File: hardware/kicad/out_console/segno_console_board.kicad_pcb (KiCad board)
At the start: 2 copper layers, 99.5 x 99.5 mm, 64 parts, among them J1 RaspberryPi_Pico_SMD_HandSold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, J10 JST_XH_B2B-XH-A_1x02_P2.50mm_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, J11 JST_XH_B2B-XH-A_1x02_P2.50mm_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, J12 JST_XH_B2B-XH-A_1x02_P2.50mm_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, J13 JST_XH_B2B-XH-A_1x02_P2.50mm_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, J14 JST_XH_B2B-XH-A_1x02_P2.50mm_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, J15 JST_XH_B2B-XH-A_1x02_P2.50mm_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, J16 JST_XH_B2B-XH-A_1x02_P2.50mm_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, J17 JST_XH_B2B-XH-A_1x02_P2.50mm_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, J18 JST_XH_B2B-XH-A_1x02_P2.50mm_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, J19 JST_XH_B2B-XH-A_1x02_P2.50mm_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, J2 IDC-Header_2x20_P2.54mm_Verti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, J20 JST_XH_B3B-XH-A_1x03_P2.50mm_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, J21 JST_XH_B3B-XH-A_1x03_P2.50mm_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, J22 PinHeader_2x04_P2.54mm_Vertic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, J3 JST_XH_B4B-XH-A_1x04_P2.50mm_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, J4 JST_XH_B3B-XH-A_1x03_P2.50mm_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, J5 JST_XH_B2B-XH-A_1x02_P2.50mm_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, J6 JST_XH_B8B-XH-A_1x08_P2.50mm_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, J7 JST_XH_B3B-XH-A_1x03_P2.50mm_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, J8 JST_XH_B2B-XH-A_1x02_P2.50mm_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, J9 JST_XH_B2B-XH-A_1x02_P2.50mm_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, U1 DIP-14_W7.62mm, U2 DIP-6_W7.62mm

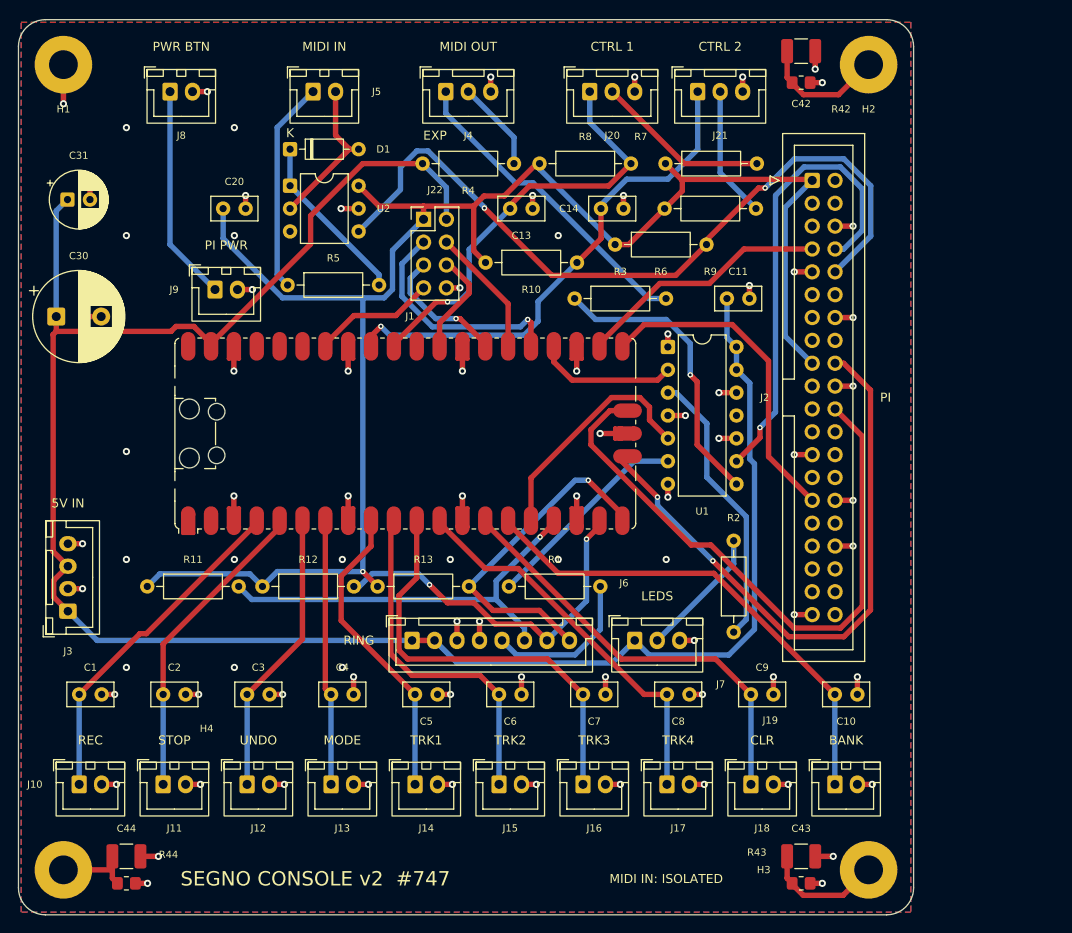
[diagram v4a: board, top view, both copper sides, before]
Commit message: fix(hardware): drop the SMD bond parts, and review the board for manufacture
The six surface-mount parts I added for the optional chassis bonds are gone.
They were a 10 nF cap and a 1 M bleeder per hole, unfitted by default, so EMC
testing could add an RF bond without a respin -- and nothing in through-hole
fits those corners, so they were SMD. That put six surface-mount parts on a
board that is hand-soldered through-hole on purpose, carried by every unit
built, for a bond that may never be wanted. H2/H3/H4 keep the plated pad and
nothing else; if a bond is ever needed a leaded cap solders from the pad to the
nearest ground via, which is a bench job on one board rather than a BOM line on
all of them. CHASSIS_BOND now gates that the other three holes are wired to
NOTHING -- a second path to ground through anything at all fails.

The only SMD left is J1, the Pico module, which is settled.

THE ENCLOSURE NOW MATCHES THE BOARD

The plate was drilling an 85 x 87 M3 rectangle measured off the V1 Pro Micro
board, while this board's holes are on 89.5 x 89.5. Both parts were unordered,
so it cost nothing -- once, and only because someone thought to look. The plate
now drills 89.5 x 89.5, reserves the real 99.5 x 99.5 outline, and the station
is labelled CONSOLE_BOARD rather than MAIN_BOARD, because the V1 board stays
with the standalone pedal.

It is a seam now, not a copied number: console_board_pcb.py writes
out_console/console_board_mount.json and segno_enclosure.py's BOARD_MOUNT gate
reads it -- the mirror of the rear_io_stations.json handoff going the other way.
Both halves of the gate were proven to bite.

WHAT THE FAB REVIEW FOUND

- Silkscreen under the fab's floor. All 58 designators were stroked at 0.133 mm
  against JLCPCB's 0.15 mm minimum, where lines thin, break, or are dropped.
  KiCad's own minimum is 0.08 mm, so its DRC had nothing to say. Stroke is now
  h/5 (0.16 mm at the 0.8 mm text height) and SILK_FAB gates height and stroke.
- Router vias at the fab f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
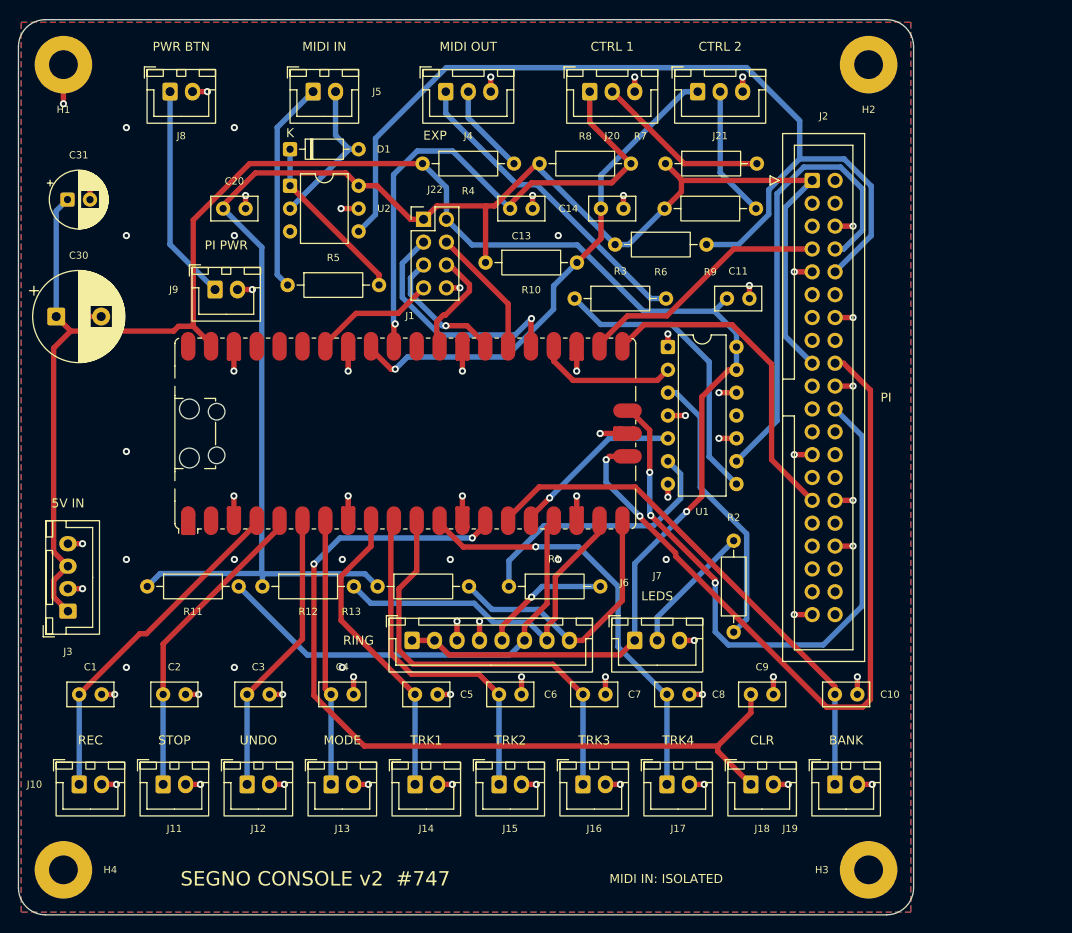
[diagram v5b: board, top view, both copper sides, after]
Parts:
- removed C42, C43, C44: C_1210_3225Metric_Pad1.33x2.70mm_HandSolder, C_1210_3225Metric_Pad1.33x2.70mm_HandSolder
- removed R42, R43, R44: R_0805_2012Metric_Pad1.20x1.40mm_HandSolder, R_0805_2012Metric_Pad1.20x1.40mm_HandSolder
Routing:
- net SW_CLEAR: track 47.7 -> 96.2 mm, vias 0 -> 2
- net MIDI_RX: track 86.0 -> 104.5 mm, vias 2 -> 0
- net SWCLK: track 67.7 -> 84.2 mm
- net CHASSIS_H2: track 14.2 -> 0.00 mm
- net CTRL1_TIP: track 47.7 -> 61.6 mm
- net CHASSIS_H3: track 13.5 -> 0.00 mm
- net GND: track 127.0 -> 117.0 mm, vias 82 -> 76
- net +5V: track 227.5 -> 218.6 mm, vias 0 -> 1
- net CHASSIS_H4: track 8.67 -> 0.00 mm
- net ENC_SW: track 37.9 -> 30.3 mm, vias 1 -> 0
- net RING_DATA: track 26.4 -> 19.3 mm, vias 0 -> 1
- net RING_DATA_BUF: track 23.4 -> 29.5 mm
- net +3V3: track 187.9 -> 182.0 mm, vias 1 -> 0
- net SW_TRACK4: track 43.4 -> 47.4 mm, vias 0 -> 1
- net ENC_A: track 46.6 -> 50.3 mm, vias 1 -> 0
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
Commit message: fix(hardware): second review pass -- close the checking gaps, not the board
The first pass found six defects and I fixed them; this pass re-reviewed the
FIXED board, deliberately looking where the first one had not. It found no
defects in the board. It found two gaps in the checking, and one blind spot
that no longer needs to exist.

THE BOARD IMPLEMENTS THE NETLIST -- now asserted, and proven to bite

Nothing checked this end to end. Every other gate compares the board to fab
limits or to itself, and DRC's unconnected check compares the board to its own
internal ratsnest, which came from the same import that could have gone wrong.
check_routed_board() now compares every pad's net against console_board.net.
Moving one pad of J6 to the wrong net makes it fail, which is the mistake it
exists to catch: a board that is DRC-clean and wired wrong.

THE SOLDER MASK RULE IS BACK ON

It was set to 0 -- off -- because 0.1in headers once produced ~100
solder_mask_bridge errors that drowned out everything else. That stopped being
true of this layout: re-enabled at the fab's own 0.25 mm, DRC comes back with
ZERO. So the blind spot goes. A rule that currently passes is worth more than
one switched off for a board we no longer have.

THE Pi LINK UART, VERIFIED RATHER THAN BELIEVED

The comment claimed GPIO4/5 was "uart2". Checked against the overlay README in
raspberrypi/linux: `uart2-pi5` is "Enable uart 2 on GPIOs 4-5. Pi 5 only." So
the wiring is right -- and the SAME PINS are uart3 on a Pi 4, where uart2 is
GPIOs 0-3. The overlay name is not portable even though the copper is, so the
firmware requirement (uart2-pi5) is now written next to the pin map.

Also checked and found clean, so recorded rather than changed:
- The 5 checks kicad-cli skips by default. Only missing_courtyard could matter
  here -- it would quietly weaken the placement gate too, which falls back to
  pad extents without a courtyard. All 58 footprints have one.
- Edge.Cuts closes into ONE outline with no inf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
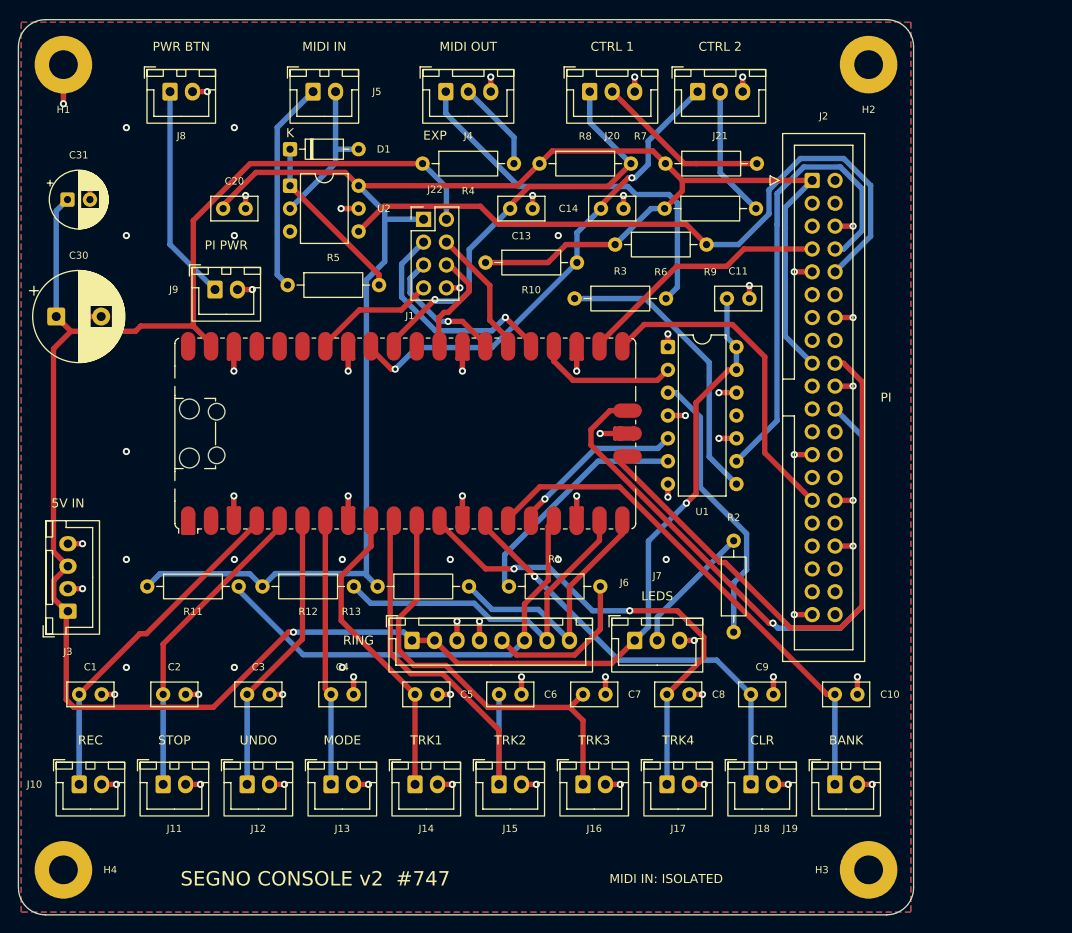
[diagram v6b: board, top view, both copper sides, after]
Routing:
- net SW_CLEAR: track 96.2 -> 47.9 mm, vias 2 -> 1
- net MIDI_RX: track 104.5 -> 77.8 mm
- net SWCLK: track 84.2 -> 65.0 mm, vias 2 -> 0
- net +5V: track 218.6 -> 236.8 mm, vias 1 -> 2
- net +3V3: track 182.0 -> 197.6 mm
- net CTRL1_TIP: track 61.6 -> 48.1 mm
- net N$1: track 35.4 -> 43.4 mm
- net SW_TRACK2: track 38.8 -> 46.6 mm
- net SW_TRACK4: track 47.4 -> 53.1 mm, vias 1 -> 2
- net RING_DATA_BUF: track 29.5 -> 26.2 mm
- net RING_DATA_OUT: track 14.3 -> 17.5 mm, vias 1 -> 0
- net SWDIO: track 71.5 -> 68.6 mm, vias 3 -> 1
- net CTRL2_TIP: track 56.0 -> 54.0 mm, vias 1 -> 2
- net EXP_GP19: track 27.1 -> 25.2 mm
- net ENC_SW: track 30.3 -> 29.4 mm
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
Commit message: fix(hardware): move the Pi link off GPIO4, which the NVMe board owns
The console does not have a bare Pi. A GeeekPi N07 NVMe board (B0CWD266XR) sits
under it, and it takes GPIO4 -- physical pin 7 -- which is exactly where the
Pi->Pico link's RX sat. That would have been a board that assembles, passes
every gate here, and cannot talk to its own MCU: two drivers on one pin, found
at first power-on with a scope, not before.

The link moves to GPIO12/13, physical pins 32/33: `dtoverlay=uart4-pi5`,
"Enable uart 4 on GPIOs 12-13. Pi 5 only." GPIO5 moves too even though nothing
was reported on it -- it is the other half of the pair the N07 sits on, and a
peripheral that claims one pin commonly claims its neighbour. Pins 32/33 are
also at the far end of the header, away from the first six positions everything
crowds into.

Nothing else collided. Pins 2/4 (5 V) are DELIBERATELY not connected here -- the
buck must not parallel the PMIC, which was already settled -- and pins 6/9 are
GND, which every board on a Pi shares by definition.

PI_RESERVED now carries the pins another board on this Pi has claimed, with WHO
claimed them, and _check() refuses to put a signal on one. Rails are exempt:
sharing 3V3 and GND is the point of a header. Its negative control puts the link
back on pin 7.

The overlay name is not portable and now says so: GPIO12/13 is uart4 on a Pi 5
and uart5 on a Pi 4, the same way GPIO4/5 was uart2 here and uart3 there.

Board: 0 DRC violations, 0 unconnected, ERC 0/0, 22 negative controls all
biting. Refs #747.
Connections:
- J2 pad 29: LINK_TX -> (no net)
- J2 pad 32: (no net) -> LINK_RX
- J2 pad 33: (no net) -> LINK_TX
- J2 pad 7: LINK_RX -> (no net)
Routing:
- net LINK_RX: track 28.3 -> 92.6 mm, vias 0 -> 2
- net SW_TRACK4: track 53.1 -> 80.1 mm, vias 2 -> 0
- net CTRL1_TIP: track 48.1 -> 67.3 mm
- net +5V: track 236.8 -> 224.7 mm, vias 2 -> 0
- net SW_TRACK3: track 48.1 -> 57.8 mm, vias 0 -> 1
- net +3V3: track 197.6 -> 189.4 mm
- net SW_CLEAR: track 47.9 -> 55.4 mm, vias 1 -> 0
- net SW_BANK: track 57.6 -> 63.2 mm, vias 0 -> 2
- net LINK_TX: track 36.5 -> 41.5 mm
- net N$1: track 43.4 -> 38.6 mm
- net EXP_GP19: track 25.2 -> 29.4 mm
- net CTRL2_TIP: track 54.0 -> 57.5 mm
- net SW_TRACK2: track 46.6 -> 43.4 mm
- net SWCLK: track 65.0 -> 67.9 mm, vias 0 -> 2
- net RING_DATA_BUF: track 26.2 -> 23.4 mm
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
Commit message: docs(hardware): why CTRL's pot and the ADC reading it sit on different rails
The pot's top is the Pi's 3V3; the ADC referencing it uses the Pico's own rail,
which the Pico 2 datasheet says is ADC_VREF 'generated on Pico 2 by filtering
the 3.3 V supply'. That makes an expression pedal the ratio of two regulators,
which reads like a bug and is worth explaining rather than rediscovering.

It stays. The same datasheet puts an inherent ~30 mV (~1%) offset on ADC_VREF
from its own 200R filter, varying with temperature and sample rate, plus SMPS
ripple in PFM mode -- so the rail mismatch is one error among several the same
size, all absorbed by the calibration an expression pedal needs anyway. The 1k
ring resistor also holds the top of travel at ~3.0 V against a ~3.27 V
reference, so the sweep cannot clip whichever rail runs high.

The encoder pull-ups on the same rail are a non-issue: they bias DIGITAL inputs,
where a valid high is a valid high.

Firmware notes recorded with it: internal pull-ups are required, and GPIO23 can
force the SMPS to PWM mode while sampling.

Refs #747.
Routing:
- net SW_TRACK4: track 80.1 -> 47.4 mm, vias 0 -> 1
- net +3V3: track 189.4 -> 214.3 mm
- net LINK_RX: track 92.6 -> 72.9 mm, vias 2 -> 1
- net CTRL1_TIP: track 67.3 -> 48.2 mm
- net SW_TRACK3: track 57.8 -> 45.9 mm, vias 1 -> 3
- net +5V: track 224.7 -> 215.8 mm
- net SWDIO: track 68.1 -> 74.3 mm, vias 1 -> 0
- net ENC_B: track 42.2 -> 37.7 mm
- net ENC_A: track 52.3 -> 47.9 mm, vias 0 -> 1
- net CTRL2_TIP: track 57.5 -> 53.3 mm
- net EXP_GP19: track 29.4 -> 25.4 mm
- net N$1: track 38.6 -> 41.2 mm
- net ENC_SW: track 30.3 -> 32.3 mm
- net SW_BANK: track 63.2 -> 61.2 mm, vias 2 -> 0
- net LINK_TX: track 41.5 -> 39.6 mm
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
